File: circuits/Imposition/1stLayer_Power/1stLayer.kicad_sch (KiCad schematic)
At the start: 4 parts, among them J1 Conn_01x14_Pin, J2 Conn_01x14_Pin, J3 Conn_01x10_Socket, J7 Conn_01x14_Pin

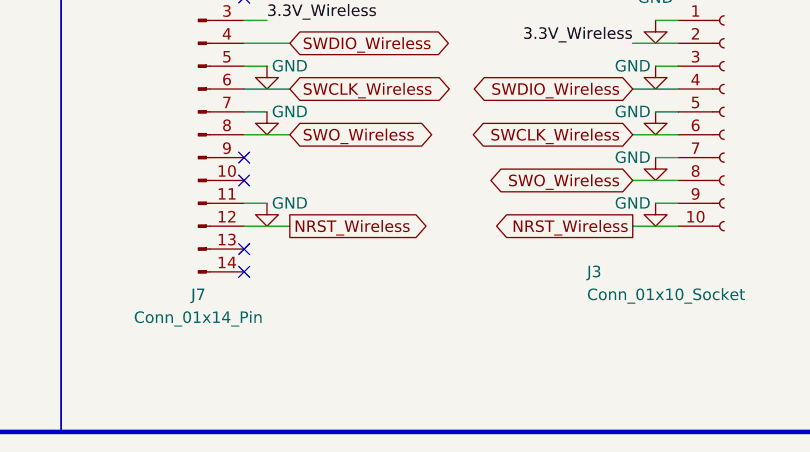
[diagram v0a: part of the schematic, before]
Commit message: 発注_第一弾
Drive, 1stLayer_Power, 2ndLayer_3rdLayer
を発注
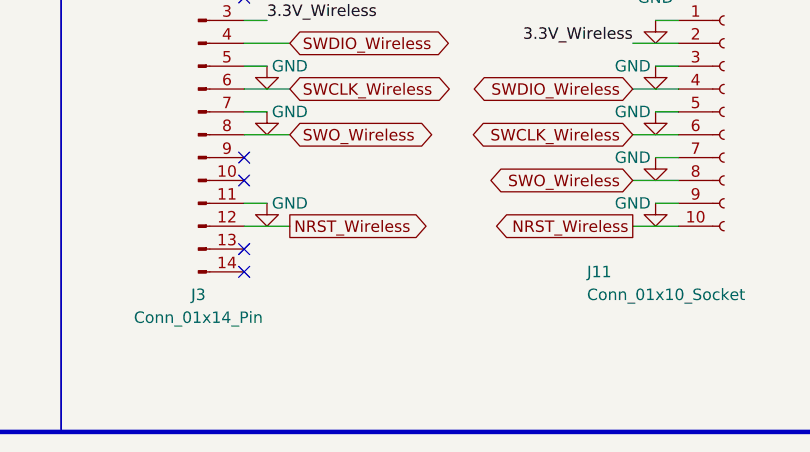
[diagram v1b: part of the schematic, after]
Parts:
- renumbered J3 to J11, J7 to J3
